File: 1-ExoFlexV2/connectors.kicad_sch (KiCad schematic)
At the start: 48 parts, among them J10 EXT, J11 EVE, J12 DOR, J13 EXT, J14 EVE_AMP_LIM, J15 DOR_AMP_LIM, J16 EXT_AMP_LIM, J17 EVE_TOR_LIM, J18 DOR_TOR_LIM, J19 EXT_TOR_LIM, J8 EVE, J9 DOR

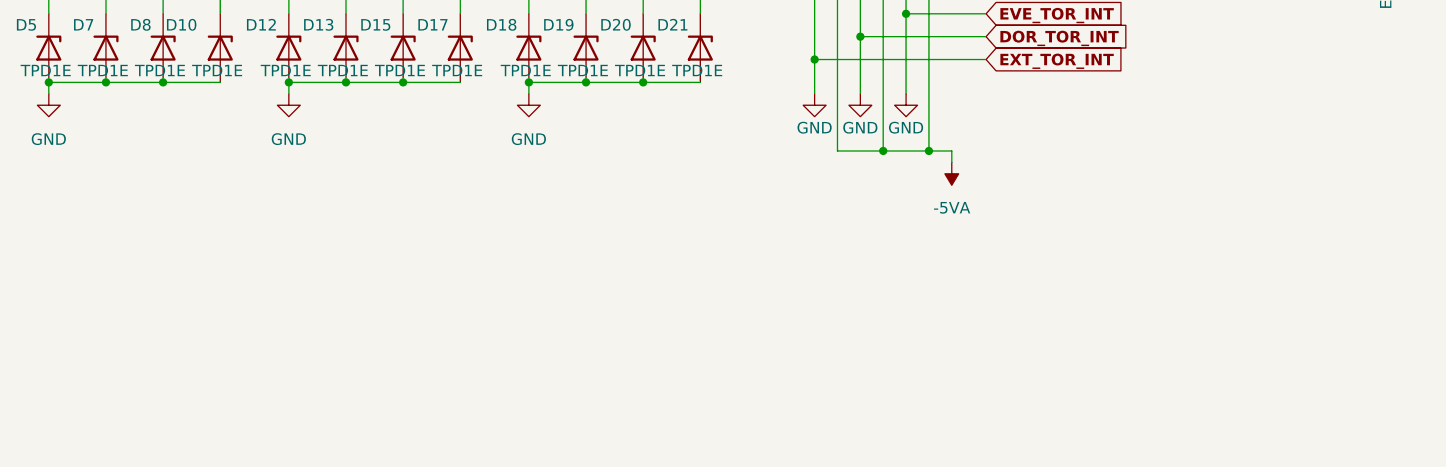
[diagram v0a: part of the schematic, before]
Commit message: Test points et notes
- Ajout de tous les tests point nécessaires
-  Ajoute des sections de notes dans chaque page
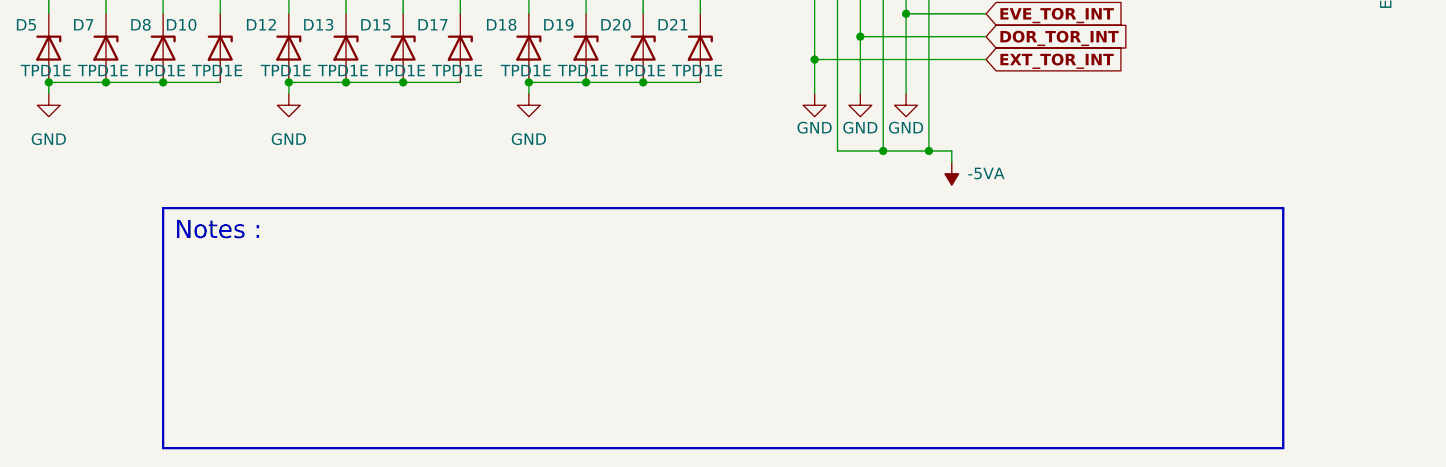
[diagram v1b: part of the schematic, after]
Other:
- note added: "Notes :"
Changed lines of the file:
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@@
     (stroke (width 0) (type default) (color 0 0 0 0))
+  )
+  (polyline (pts (xy 48.26 168.91) (xy 48.26 195.58))
+    (stroke (width 0.25) (type solid) (color 0 0 0 0))
   )
   (wire (pts (xy 153.67 72.39) (xy 160.02 72.39))
@@
     (stroke (width 0) (type default) (color 0 0 0 0))
   )
+  (polyline (pts (xy 48.26 168.91) (xy 172.72 168.91))
+    (stroke (width 0.25) (type solid) (color 0 0 0 0))
+  )
   (wire (pts (xy 25.4 106.68) (xy 88.9 106.68))
     (stroke (width 0) (type default) (color 0 0 0 0))
+  )
+  (polyline (pts (xy 172.72 195.58) (xy 48.26 195.58))
+    (stroke (width 0.25) (type solid) (color 0 0 0 0))
   )
   (wire (pts (xy 52.07 74.93) (xy 58.42 74.93))
@@
   (polyline (pts (xy 220.98 40.64) (xy 281.94 40.64))
     (stroke (width 0.5) (type dash) (color 255 148 44 1))
+  )
+  (polyline (pts (xy 172.72 168.91) (xy 172.72 195.58))
+    (stroke (width 0.25) (type solid) (color 0 0 0 0))
   )
   (wire (pts (xy 125.73 149.86) (xy 139.7 149.86))
@@
   (text "AMPLITUDE" (at 12.7 15.24 0)
     (effects (font (size 1.5 1.5) (thickness 0.3) bold) (justify left bottom))
+  )
+  (text "Notes :" (at 49.53 172.72 0)
+    (effects (font (size 2 2)) (justify left bottom))
   )
   (global_label "EXT_AMP_LIM" (shape input) (at 187.96 60.96 0) (fields_autoplaced)
@@
   )
   (symbol (lib_id "power:-5VA") (at 135.89 163.83 180) (unit 1)
-    (in_bom yes) (on_board yes) (fields_autoplaced)
+    (in_bom yes) (on_board yes)
     (property "Reference" "#PWR050" (id 0) (at 135.89 166.37 0)
       (effects (font (size 1.27 1.27)) hide)
     )
-    (property "Value" "-5VA" (id 1) (at 135.89 168.91 0))
+    (property "Value" "-5VA" (id 1) (at 139.7 165.1 0))
     (property "Footprint" "" (id 2) (at 135.89 163.83 0)
       (effects (font (size 1.27 1.27)) hide)

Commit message: Schématisation terminée
- Schéma terminé
- Passage vers le PCB
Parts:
- D10: renamed from D11; value TPD1E -> TVS; DESCRIPTION (none) -> TVS DIODE 5.5VWM 14VC 2X1SON; MANUFACTURER (none) -> Texas Instruments; PACKAGE (none) -> 0402 (1006 Metric); PART NUMBER (none) -> TPD1E05U06DPYR; TYPE (none) -> SMD
- D11: renamed from D12; value TPD1E -> TVS; DESCRIPTION (none) -> TVS DIODE 5.5VWM 14VC 2X1SON; MANUFACTURER (none) -> Texas Instruments; PACKAGE (none) -> 0402 (1006 Metric); PART NUMBER (none) -> TPD1E05U06DPYR; TYPE (none) -> SMD
- D12: renamed from D13; value TPD1E -> TVS; DESCRIPTION (none) -> TVS DIODE 5.5VWM 14VC 2X1SON; MANUFACTURER (none) -> Texas Instruments; PACKAGE (none) -> 0402 (1006 Metric); PART NUMBER (none) -> TPD1E05U06DPYR; TYPE (none) -> SMD
- D13: renamed from D14; value TPD1E -> TVS; DESCRIPTION (none) -> TVS DIODE 5.5VWM 14VC 2X1SON; MANUFACTURER (none) -> Texas Instruments; PACKAGE (none) -> 0402 (1006 Metric); PART NUMBER (none) -> TPD1E05U06DPYR; TYPE (none) -> SMD
- D14: renamed from D15; value TPD1E -> TVS; DESCRIPTION (none) -> TVS DIODE 5.5VWM 14VC 2X1SON; MANUFACTURER (none) -> Texas Instruments; PACKAGE (none) -> 0402 (1006 Metric); PART NUMBER (none) -> TPD1E05U06DPYR; TYPE (none) -> SMD
- D15: renamed from D16; value TPD1E -> TVS; DESCRIPTION (none) -> TVS DIODE 5.5VWM 14VC 2X1SON; MANUFACTURER (none) -> Texas Instruments; PACKAGE (none) -> 0402 (1006 Metric); PART NUMBER (none) -> TPD1E05U06DPYR; TYPE (none) -> SMD
- D16: renamed from D17; value TPD1E -> TVS; DESCRIPTION (none) -> TVS DIODE 5.5VWM 14VC 2X1SON; MANUFACTURER (none) -> Texas Instruments; PACKAGE (none) -> 0402 (1006 Metric); PART NUMBER (none) -> TPD1E05U06DPYR; TYPE (none) -> SMD
- D17: renamed from D18; value TPD1E -> TVS; DESCRIPTION (none) -> TVS DIODE 5.5VWM 14VC 2X1SON; MANUFACTURER (none) -> Texas Instruments; PACKAGE (none) -> 0402 (1006 Metric); PART NUMBER (none) -> TPD1E05U06DPYR; TYPE (none) -> SMD
- D18: renamed from D19; value TPD1E -> TVS; DESCRIPTION (none) -> TVS DIODE 5.5VWM 14VC 2X1SON; MANUFACTURER (none) -> Texas Instruments; PACKAGE (none) -> 0402 (1006 Metric); PART NUMBER (none) -> TPD1E05U06DPYR; TYPE (none) -> SMD
- D19: renamed from D20; value TPD1E -> TVS; DESCRIPTION (none) -> TVS DIODE 5.5VWM 14VC 2X1SON; MANUFACTURER (none) -> Texas Instruments; PACKAGE (none) -> 0402 (1006 Metric); PART NUMBER (none) -> TPD1E05U06DPYR; TYPE (none) -> SMD
- D20: renamed from D21; value TPD1E -> TVS; DESCRIPTION (none) -> TVS DIODE 5.5VWM 14VC 2X1SON; MANUFACTURER (none) -> Texas Instruments; PACKAGE (none) -> 0402 (1006 Metric); PART NUMBER (none) -> TPD1E05U06DPYR; TYPE (none) -> SMD
- D21: renamed from D22; value TPD1E -> TVS; DESCRIPTION (none) -> TVS DIODE 5.5VWM 14VC 2X1SON; MANUFACTURER (none) -> Texas Instruments; PACKAGE (none) -> 0402 (1006 Metric); PART NUMBER (none) -> TPD1E05U06DPYR; TYPE (none) -> SMD
- D22: renamed from D23; value TPD1E -> TVS; DESCRIPTION (none) -> TVS DIODE 5.5VWM 14VC 2X1SON; MANUFACTURER (none) -> Texas Instruments; PACKAGE (none) -> 0402 (1006 Metric); PART NUMBER (none) -> TPD1E05U06DPYR; TYPE (none) -> SMD
- D23: renamed from D24; value TPD1E -> TVS; DESCRIPTION (none) -> TVS DIODE 5.5VWM 14VC 2X1SON; MANUFACTURER (none) -> Texas Instruments; PACKAGE (none) -> 0402 (1006 Metric); PART NUMBER (none) -> TPD1E05U06DPYR; TYPE (none) -> SMD
- D24: renamed from D25; value TPD1E -> TVS; DESCRIPTION (none) -> TVS DIODE 5.5VWM 14VC 2X1SON; MANUFACTURER (none) -> Texas Instruments; PACKAGE (none) -> 0402 (1006 Metric); PART NUMBER (none) -> TPD1E05U06DPYR; TYPE (none) -> SMD
- D25: renamed from D26; value TPD1E -> TVS; DESCRIPTION (none) -> TVS DIODE 5.5VWM 14VC 2X1SON; MANUFACTURER (none) -> Texas Instruments; PACKAGE (none) -> 0402 (1006 Metric); PART NUMBER (none) -> TPD1E05U06DPYR; TYPE (none) -> SMD
- D26: renamed from D27; value TPD1E -> TVS; DESCRIPTION (none) -> TVS DIODE 5.5VWM 14VC 2X1SON; MANUFACTURER (none) -> Texas Instruments; PACKAGE (none) -> 0402 (1006 Metric); PART NUMBER (none) -> TPD1E05U06DPYR; TYPE (none) -> SMD
- D27: renamed from D28; value TPD1E -> TVS; DESCRIPTION (none) -> TVS DIODE 5.5VWM 14VC 2X1SON; MANUFACTURER (none) -> Texas Instruments; PACKAGE (none) -> 0402 (1006 Metric); PART NUMBER (none) -> TPD1E05U06DPYR; TYPE (none) -> SMD
- D28: renamed from D29; value TPD1E -> TVS; DESCRIPTION (none) -> TVS DIODE 5.5VWM 14VC 2X1SON; MANUFACTURER (none) -> Texas Instruments; PACKAGE (none) -> 0402 (1006 Metric); PART NUMBER (none) -> TPD1E05U06DPYR; TYPE (none) -> SMD
- D29: renamed from D30; value TPD1E -> TVS; DESCRIPTION (none) -> TVS DIODE 5.5VWM 14VC 2X1SON; MANUFACTURER (none) -> Texas Instruments; PACKAGE (none) -> 0402 (1006 Metric); PART NUMBER (none) -> TPD1E05U06DPYR; TYPE (none) -> SMD
- D3: renamed from D4; value TPD1E -> TVS; DESCRIPTION (none) -> TVS DIODE 5.5VWM 14VC 2X1SON; MANUFACTURER (none) -> Texas Instruments; PACKAGE (none) -> 0402 (1006 Metric); PART NUMBER (none) -> TPD1E05U06DPYR; TYPE (none) -> SMD
- D30: renamed from D31; value TPD1E -> TVS; DESCRIPTION (none) -> TVS DIODE 5.5VWM 14VC 2X1SON; MANUFACTURER (none) -> Texas Instruments; PACKAGE (none) -> 0402 (1006 Metric); PART NUMBER (none) -> TPD1E05U06DPYR; TYPE (none) -> SMD
- D31: renamed from D32; value TPD1E -> TVS; DESCRIPTION (none) -> TVS DIODE 5.5VWM 14VC 2X1SON; MANUFACTURER (none) -> Texas Instruments; PACKAGE (none) -> 0402 (1006 Metric); PART NUMBER (none) -> TPD1E05U06DPYR; TYPE (none) -> SMD
- D32: renamed from D33; value TPD1E -> TVS; DESCRIPTION (none) -> TVS DIODE 5.5VWM 14VC 2X1SON; MANUFACTURER (none) -> Texas Instruments; PACKAGE (none) -> 0402 (1006 Metric); PART NUMBER (none) -> TPD1E05U06DPYR; TYPE (none) -> SMD
- D33: renamed from D34; value TPD1E -> TVS; DESCRIPTION (none) -> TVS DIODE 5.5VWM 14VC 2X1SON; MANUFACTURER (none) -> Texas Instruments; PACKAGE (none) -> 0402 (1006 Metric); PART NUMBER (none) -> TPD1E05U06DPYR; TYPE (none) -> SMD
- D34: renamed from D35; value TPD1E -> TVS; DESCRIPTION (none) -> TVS DIODE 5.5VWM 14VC 2X1SON; MANUFACTURER (none) -> Texas Instruments; PACKAGE (none) -> 0402 (1006 Metric); PART NUMBER (none) -> TPD1E05U06DPYR; TYPE (none) -> SMD
- D35: renamed from D36; value TPD1E -> TVS; DESCRIPTION (none) -> TVS DIODE 5.5VWM 14VC 2X1SON; MANUFACTURER (none) -> Texas Instruments; PACKAGE (none) -> 0402 (1006 Metric); PART NUMBER (none) -> TPD1E05U06DPYR; TYPE (none) -> SMD
- D36: renamed from D37; value TPD1E -> TVS; DESCRIPTION (none) -> TVS DIODE 5.5VWM 14VC 2X1SON; MANUFACTURER (none) -> Texas Instruments; PACKAGE (none) -> 0402 (1006 Metric); PART NUMBER (none) -> TPD1E05U06DPYR; TYPE (none) -> SMD
- D37: renamed from D38; value TPD1E -> TVS; DESCRIPTION (none) -> TVS DIODE 5.5VWM 14VC 2X1SON; MANUFACTURER (none) -> Texas Instruments; PACKAGE (none) -> 0402 (1006 Metric); PART NUMBER (none) -> TPD1E05U06DPYR; TYPE (none) -> SMD
- D38: renamed from D39; value TPD1E -> TVS; DESCRIPTION (none) -> TVS DIODE 5.5VWM 14VC 2X1SON; MANUFACTURER (none) -> Texas Instruments; PACKAGE (none) -> 0402 (1006 Metric); PART NUMBER (none) -> TPD1E05U06DPYR; TYPE (none) -> SMD
- D4: renamed from D5; value TPD1E -> TVS; DESCRIPTION (none) -> TVS DIODE 5.5VWM 14VC 2X1SON; MANUFACTURER (none) -> Texas Instruments; PACKAGE (none) -> 0402 (1006 Metric); PART NUMBER (none) -> TPD1E05U06DPYR; TYPE (none) -> SMD
- D5: renamed from D6; value TPD1E -> TVS; DESCRIPTION (none) -> TVS DIODE 5.5VWM 14VC 2X1SON; MANUFACTURER (none) -> Texas Instruments; PACKAGE (none) -> 0402 (1006 Metric); PART NUMBER (none) -> TPD1E05U06DPYR; TYPE (none) -> SMD
- D6: renamed from D7; value TPD1E -> TVS; DESCRIPTION (none) -> TVS DIODE 5.5VWM 14VC 2X1SON; MANUFACTURER (none) -> Texas Instruments; PACKAGE (none) -> 0402 (1006 Metric); PART NUMBER (none) -> TPD1E05U06DPYR; TYPE (none) -> SMD
- D7: renamed from D8; value TPD1E -> TVS; DESCRIPTION (none) -> TVS DIODE 5.5VWM 14VC 2X1SON; MANUFACTURER (none) -> Texas Instruments; PACKAGE (none) -> 0402 (1006 Metric); PART NUMBER (none) -> TPD1E05U06DPYR; TYPE (none) -> SMD
- D8: renamed from D9; value TPD1E -> TVS; DESCRIPTION (none) -> TVS DIODE 5.5VWM 14VC 2X1SON; MANUFACTURER (none) -> Texas Instruments; PACKAGE (none) -> 0402 (1006 Metric); PART NUMBER (none) -> TPD1E05U06DPYR; TYPE (none) -> SMD
- D9: renamed from D10; value TPD1E -> TVS; DESCRIPTION (none) -> TVS DIODE 5.5VWM 14VC 2X1SON; MANUFACTURER (none) -> Texas Instruments; PACKAGE (none) -> 0402 (1006 Metric); PART NUMBER (none) -> TPD1E05U06DPYR; TYPE (none) -> SMD
- J13: renamed from J8; value EVE -> 3; DESCRIPTION (none) -> 3 Position Wire to Board Terminal Block 55° (125°) Angle wi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; PACKAGE (none) -> 3 POS 0.100" (2.54mm); PART NUMBER (none) -> 1751109; TYPE (none) -> Through Hole
- J14: renamed from J9; value DOR -> 3; DESCRIPTION (none) -> 3 Position Wire to Board Terminal Block 55° (125°) Angle wi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; PACKAGE (none) -> 3 POS 0.100" (2.54mm); PART NUMBER (none) -> 1751109; TYPE (none) -> Through Hole
- J15: renamed from J10; value EXT -> 3; DESCRIPTION (none) -> 3 Position Wire to Board Terminal Block 55° (125°) Angle wi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; PACKAGE (none) -> 3 POS 0.100" (2.54mm); PART NUMBER (none) -> 1751109; TYPE (none) -> Through Hole
- J16: renamed from J11; value EVE -> 5; DESCRIPTION (none) -> 5 Position Wire to Board Terminal Block 55° (125°) Angle wi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; PACKAGE (none) -> 5 POS 0.100" (2.54mm); PART NUMBER (none) -> 1751125; TYPE (none) -> Through Hole
- J17: renamed from J12; value DOR -> 5; DESCRIPTION (none) -> 5 Position Wire to Board Terminal Block 55° (125°) Angle wi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; PACKAGE (none) -> 5 POS 0.100" (2.54mm); PART NUMBER (none) -> 1751125; TYPE (none) -> Through Hole
- J18: renamed from J13; value EXT -> 5; DESCRIPTION (none) -> 5 Position Wire to Board Terminal Block 55° (125°) Angle wi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; PACKAGE (none) -> 5 POS 0.100" (2.54mm); PART NUMBER (none) -> 1751125; TYPE (none) -> Through Hole
- J19: renamed from J14; value EVE_AMP_LIM -> 3; DESCRIPTION (none) -> 3 Position Wire to Board Terminal Block 55° (125°) Angle wi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; PACKAGE (none) -> 3 POS 0.100" (2.54mm); PART NUMBER (none) -> 1751109; TYPE (none) -> Through Hole
- J20: renamed from J15; value DOR_AMP_LIM -> 3; DESCRIPTION (none) -> 3 Position Wire to Board Terminal Block 55° (125°) Angle wi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; PACKAGE (none) -> 3 POS 0.100" (2.54mm); PART NUMBER (none) -> 1751109; TYPE (none) -> Through Hole
- J21: renamed from J16; value EXT_AMP_LIM -> 3; DESCRIPTION (none) -> 3 Position Wire to Board Terminal Block 55° (125°) Angle wi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; PACKAGE (none) -> 3 POS 0.100" (2.54mm); PART NUMBER (none) -> 1751109; TYPE (none) -> Through Hole
- J22: renamed from J17; value EVE_TOR_LIM -> 3; DESCRIPTION (none) -> 3 Position Wire to Board Terminal Block 55° (125°) Angle wi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; PACKAGE (none) -> 3 POS 0.100" (2.54mm); PART NUMBER (none) -> 1751109; TYPE (none) -> Through Hole
- J23: renamed from J18; value DOR_TOR_LIM -> 3; DESCRIPTION (none) -> 3 Position Wire to Board Terminal Block 55° (125°) Angle wi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; PACKAGE (none) -> 3 POS 0.100" (2.54mm); PART NUMBER (none) -> 1751109; TYPE (none) -> Through Hole
- J24: renamed from J19; value EXT_TOR_LIM -> 3; DESCRIPTION (none) -> 3 Position Wire to Board Terminal Block 55° (125°) Angle wi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; PACKAGE (none) -> 3 POS 0.100" (2.54mm); PART NUMBER (none) -> 1751109; TYPE (none) -> Through Hole
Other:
- note added: "4xMagEncoder : 5VA @ 26mA 3xTorSensor : ±5VA @ 39,47mA Total current : 5VA @ 70mA -5VA @ 44mA"
- note added: "Dorsiflexion"
- note added: "Extension"
- note added: "Limite Amplitude Dorsiflexion"
- note added: "Limite Amplitude Extension"
- note added: "Limite Amplitude Éversion"
- note added: "Limite Torque Dorsiflexion"
- note added: "Limite Torque Extension"
- note added: "Limite Torque Éversion"
- note added: "Éversion"
- note removed: "5xMagEncoder : 5VA @ 32,5mA 3xTorSensor : ±5VA @ 20,55mA Total current : 5VA @ 53,05mA -5VA @ 20,55mA"

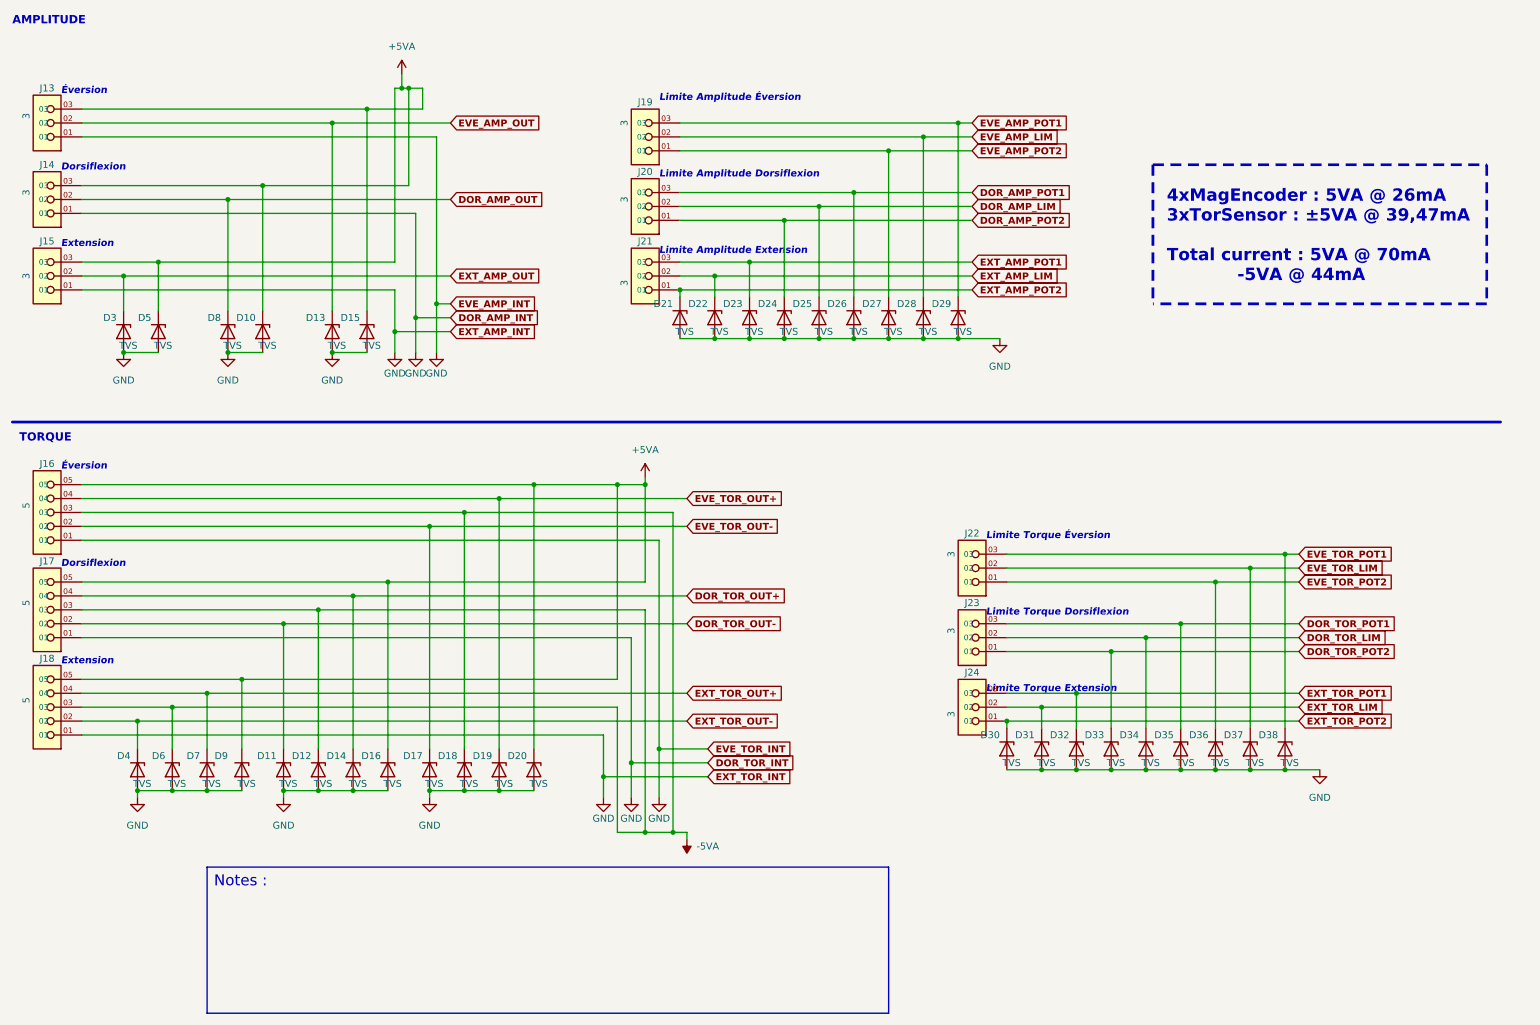
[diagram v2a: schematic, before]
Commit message: Bug NetList
- Ajout de net-tie pour les GND et et les +5V
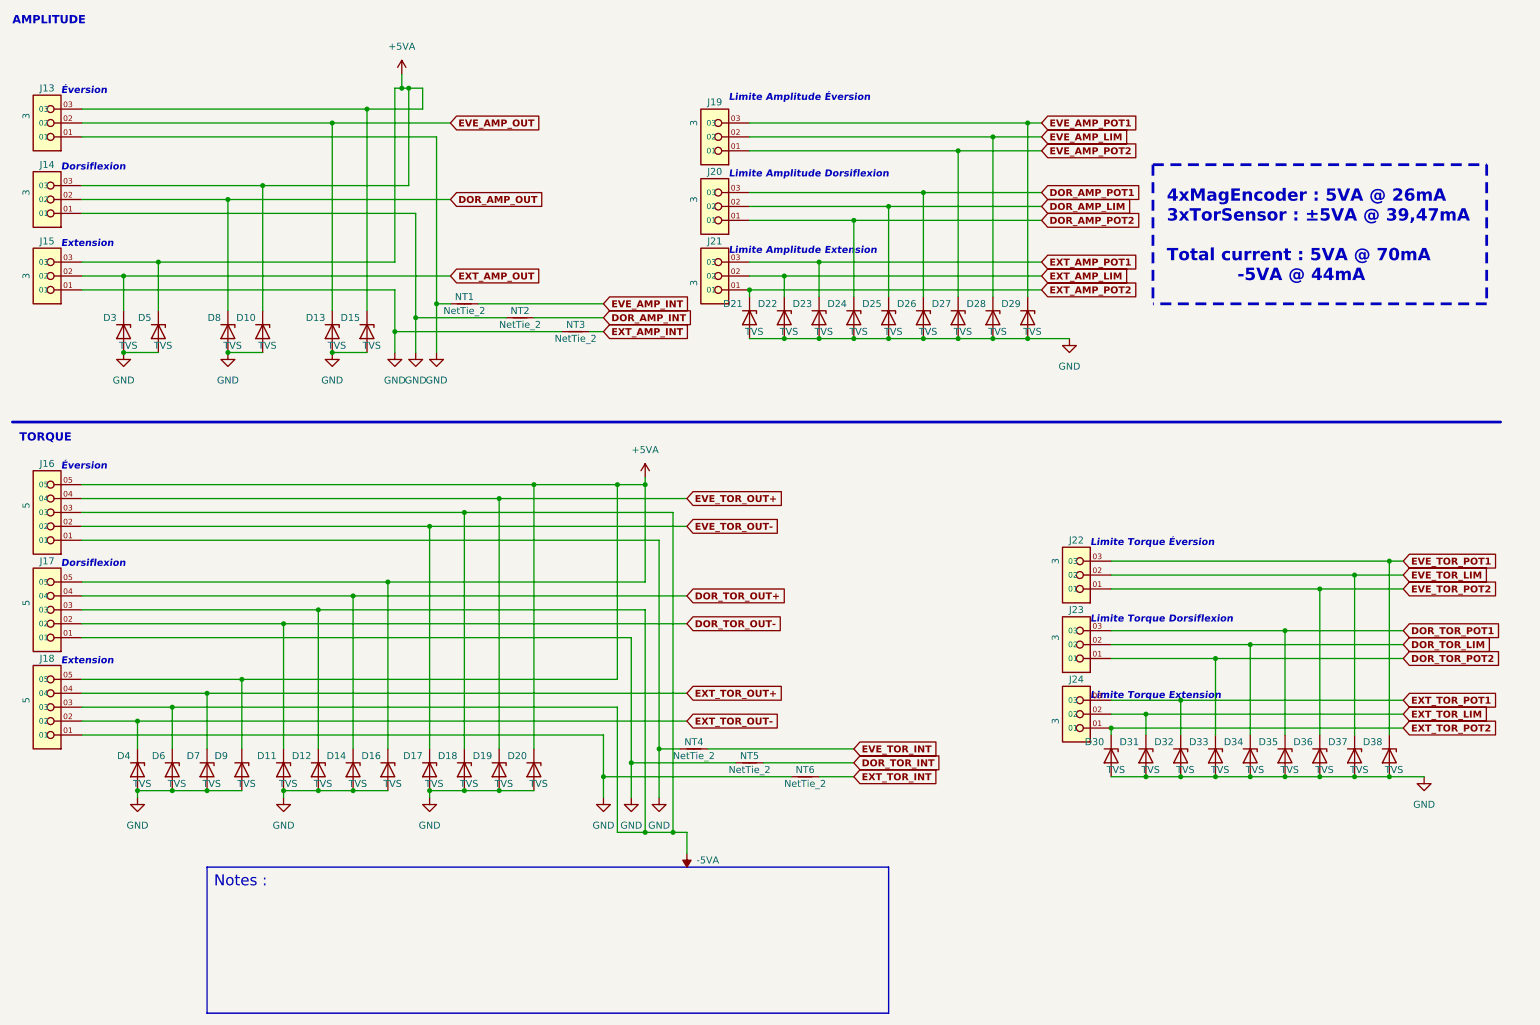
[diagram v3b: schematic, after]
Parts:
- added NT1, NT2, NT3, NT4, NT5, NT6: NetTie_2, NetTie:NetTie-2_SMD_Pad0.5mm, symbol Device:NetTie_2
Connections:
- net GND: now also NT1.1, NT2.1, NT3.1, NT4.1, NT5.1, NT6.1
- new net DOR_AMP_INT: NT2.2
- new net DOR_TOR_INT: NT5.2
- new net EVE_AMP_INT: NT1.2
- new net EVE_TOR_INT: NT4.2
- new net EXT_AMP_INT: NT3.2
- new net EXT_TOR_INT: NT6.2
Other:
- moved on the sheet: D21, D22, D23, D24, D25, D26, D27, D28, D29, D30, D31, D32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
